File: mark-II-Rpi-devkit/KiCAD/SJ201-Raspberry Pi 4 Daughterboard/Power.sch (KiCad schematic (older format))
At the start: 36 parts, among them J1 Barrel_Jack, J5 PowerTP, Q3 AO3401A, U1 XL4501E1, U2 NCP303LSN09, U4 AMS1117-3.3, U7 MP2359

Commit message: SJ-201 v3, sent to PCB Fab. Removed USB Hub, add in I2S to Line Out
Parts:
- C1: Tempo (none) -> UCD1H221MNL1GS
- C2: Tempo (none) -> C0402C222K5RACTU
- C6: SKU 508000001 -> (none); Tempo (none) -> 25TKV330M8X10.5
- C64: Tempo (none) -> EEE-1CA471UP
- C8: SKU 508000001 -> (none)
- D14: Tempo (none) -> SS54-HF
- D15: Tempo (none) -> B5819W-TP
- FB8: Tempo (none) -> BK32164S301-T
- L1: Tempo (none) -> VCMT136E-470MN5
- L2: Tempo (none) -> BRL3225T2R2M
- PWR1: Tempo (none) -> 19-217/R6C-AL1M2VY/3T
- R27: Tempo (none) -> ERJ-2GEJ104X
- R28: Tempo (none) -> RC0402JR-07680RL
- R3: Tempo (none) -> RC0402FR-0775KL
- R4: Tempo (none) -> RC0402FR-07330KL
- R8: Tempo (none) -> RC0402FR-073K3L
- U4: value AMS1117-3.3 -> NCP565; Link (none) -> https://lcsc.com/product-detail/Dropout-Regulators-LDO_ON-S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; MPN AMS1117-3.3 -> NCP565ST12T3G; Tempo (none) -> NCP565ST12T3G
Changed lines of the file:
@@
 Sheet 2 6
 Title "Power"
-Date "2020-09-26"
-Rev "0.67b"
+Date "2020-10-02"
+Rev "0.67c"
 Comp "Mycroft"
 Comment1 "Power Converter"
@@
 F 5 "https://lcsc.com/product-detail/Power-Inductors_TDG-TMAX-1365-470-M_C429835.html" V 4275 3075 50  0001 C CNN "Link"
 F 6 "C429835" H 4275 3075 50  0001 C CNN "LCSC"
+F 7 "VCMT136E-470MN5" H 4275 3075 50  0001 C CNN "Tempo"
 	1    4275 3075
 	0    -1   -1   0
@@
 F 4 "0402WGF3301TCE" H 5475 3525 50  0001 C CNN "MPN"
 F 5 "C25890" H 5475 3525 50  0001 C CNN "LCSC"
+F 6 "RC0402FR-073K3L" H 5475 3525 50  0001 C CNN "Tempo"
 	1    5475 3525
 	-1   0    0    1
@@
 F 4 "RVT1E331M0810" H 4880 3575 20  0001 C CNN "MPN"
 F 5 "C74593-DNP" H 4850 3425 50  0001 C CNN "LCSC"
-F 6 "508000001" H 4850 3425 50  0001 C CNN "SKU"
+F 6 "25TKV330M8X10.5" H 4850 3425 50  0001 C CNN "Tempo"
 	1    4850 3425
 	1    0    0    -1
@@
 F 4 "GRM155R71A333KA01D" H 5855 3375 20  0001 C CNN "MPN"
 F 5 "C1585" H 5825 3225 50  0001 C CNN "LCSC"
-F 6 "508000001" H 5825 3225 50  0001 C CNN "SKU"
 	1    5825 3225
 	1    0    0    -1
@@
 F 5 "301010033" H 8850 1575 50  0001 C CNN "SKU"
 F 6 "C25741" H 8850 1575 50  0001 C CNN "LCSC"
+F 7 "ERJ-2GEJ104X" H 8850 1575 50  0001 C CNN "Tempo"
 	1    8850 1575
 	1    0    0    -1
@@
 P 1925 4750
 F 0 "U4" H 1925 4992 50  0000 C CNN
-F 1 "AMS1117-3.3" H 1925 4901 50  0000 C CNN
+F 1 "NCP565" H 1925 4901 50  0000 C CNN
 F 2 "Package_TO_SOT_SMD:SOT-223-3_TabPin2" H 1925 5000 50  0001 C CIN
 F 3 "" H 1925 4750 50  0001 C CNN
-F 4 "AMS1117-3.3" H 1925 4750 50  0001 C CNN "MPN"
-F 5 "C6186" H 1925 4750 50  0001 C CNN "LCSC"
+F 4 "NCP565ST12T3G" H 1925 4750 50  0001 C CNN "MPN"
+F 5 "NCP565ST12T3G" H 1925 4750 50  0001 C CNN "Tempo"
+F 6 "C6186" H 1925 4750 50  0001 C CNN "LCSC"
+F 7 "https://lcsc.com/product-detail/Dropout-Regulators-LDO_ON-Semiconductor-ON-NCP565ST12T3G_C556400.html" H 1925 4750 50  0001 C CNN "Link"
 	1    1925 4750
 	1    0    0    -1
@@
 F 6 "https://lcsc.com/product-detail/Others_TOGIALED-TJ-S1608SW6TGLC2R-A5_C192315.html" V 6650 3425 50  0001 C CNN "Link"
 F 7 "304090042" H 6650 3425 50  0001 C CNN "SKU"
+F 8 "19-217/R6C-AL1M2VY/3T" H 6650 3425 50  0001 C CNN "Tempo"
 	1    6650 3425
 	0    -1   -1   0
@@
 F 5 "Chip Resistor - Surface Mount 680Ohms ±1% 1/16W 0402 RoHS" H 6650 3175 50  0001 C CNN "Desc"
 F 6 "0402WGF6800TCE" H 6650 3175 50  0001 C CNN "MPN"
+F 7 "RC0402JR-07680RL" H 6650 3175 50  0001 C CNN "Tempo"
 	1    6650 3175
 	-1   0    0    1
@@
 F 4 "MLB3216-301P3A(f)" H 8350 1175 50  0001 C CNN "MPN"
 F 5 "C29107" H 8350 1175 50  0001 C CNN "LCSC"
+F 6 "BK32164S301-T" H 8350 1175 50  0001 C CNN "Tempo"
 	1    8350 1175
 	0    -1   1    0
@@
 F 5 "302030006" H 9280 1525 20  0001 C CNN "SKU"
 F 6 "C176671-DNP" H 9250 1375 50  0001 C CNN "LCSC"
+F 7 "EEE-1CA471UP" H 9250 1375 50  0001 C CNN "Tempo"
 	1    9250 1375
 	1    0    0    -1
@@
 F 4 "SS54F" H 3900 3250 50  0001 C CNN "MPN"
 F 5 "C22452" H 3900 3250 50  0001 C CNN "LCSC"
+F 6 "SS54-HF" H 3900 3250 50  0001 C CNN "Tempo"
 	1    3900 3250
 	0    1    1    0
@@
 F 7 "https://lcsc.com/product-detail/Aluminum-Electrolytic-Capacitors-SMD_Lelon-VZH221M1HTR-1010_C134819.html/?href=jlc-SMT" H 1600 3275 50  0001 C CNN "Link"
 F 8 "LCSC" H 1600 3275 50  0001 C CNN "Vendor"
+F 9 "UCD1H221MNL1GS" H 1600 3275 50  0001 C CNN "Tempo"
 	1    1600 3275
 	1    0    0    -1
@@
 F 4 "C25798" H 4325 6700 50  0001 C CNN "LCSC"
 F 5 "0402WGF7502TCE" H 4325 6700 50  0001 C CNN "MPN"
+F 6 "RC0402FR-0775KL" H 4325 6700 50  0001 C CNN "Tempo"
 	1    4325 6700
 	1    0    0    -1
@@
 F 4 "C86074" H 3825 6550 50  0001 C CNN "LCSC"
 F 5 "LQH32PN2R2NN0L" H 3825 6550 50  0001 C CNN "MPN"
+F 6 "BRL3225T2R2M" H 3825 6550 50  0001 C CNN "Tempo"
 	1    3825 6550
 	0    -1   -1   0
@@
 F 4 "C25778" H 4325 7050 50  0001 C CNN "LCSC"
 F 5 "0402WGF3303TCE" H 4325 7050 50  0001 C CNN "MPN"
+F 6 "RC0402FR-07330KL" H 4325 7050 50  0001 C CNN "Tempo"
 	1    4325 7050
 	-1   0    0    1
@@
 F 4 "B5819W" H 3400 6700 50  0001 C CNN "MPN"
 F 5 "C8598" H 3400 6700 50  0001 C CNN "LCSC"
+F 6 "B5819W-TP" H 3400 6700 50  0001 C CNN "Tempo"
 	1    3400 6700
 	0    1    1    0
@@
 F 6 "https://lcsc.com/product-detail/Multilayer-Ceramic-Capacitors-MLCC-SMD-SMT_2-2nF-222-10-50V_C1531.html/?href=jlc-SMT" H 3350 5200 50  0001 C CNN "Link"
 F 7 "LCSC" H 3350 5200 50  0001 C CNN "Vendor"
+F 8 "C0402C222K5RACTU" H 3350 5200 50  0001 C CNN "Tempo"
 	1    3350 5200
 	-1   0    0    -1

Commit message: Rev4 Update - Add in Coral TPU, TAS5806, remove I2S * MAX9744. Change Attiny to Attin1614
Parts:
- removed C2: 2.2NF, Capacitor_SMD:C_0402_1005Metric, symbol Device:C_Small
- removed C9: 1NF, Capacitor_SMD:C_0402_1005Metric, symbol Device:C_Small
- removed R2: 10k, Resistor_SMD:R_0402_1005Metric, symbol Device:R_Small
- removed TP25: TestPoint, TestPoint:TestPoint_Pad_D2.0mm, symbol Connector:TestPoint
- removed U2: NCP303LSN09, Package_TO_SOT_SMD:SOT-23-5, symbol user:NCP303LSN30
- added C66: 1uF, Capacitor_Tantalum_SMD:CP_EIA-3216-10_Kemet-I, symbol Device:CP1_Small
- added C67: 470uF, Capacitor_Tantalum_SMD:CP_EIA-7343-15_Kemet-W, symbol Device:CP
- added R51: 3.3K, Resistor_SMD:R_0402_1005Metric, symbol Device:R_Small
- added TP12v1: TestPoint, TestPoint:TestPoint_Pad_D2.0mm, symbol Connector:TestPoint
- added U12: TPS75933KTT, Package_TO_SOT_SMD:TO-263-5_TabPin3, symbol user:TPS759xxx
- J5: footprint Connector_PinHeader_2.54mm:PinHeader_2x04_P2.54mm_Vertical -> Connector_PinHeader_1.27mm:PinHeader_1x06_P1.27mm_Vertical_SMD_Pin1Left; symbol Connector_Generic:Conn_02x04_Odd_Even -> Connector_Generic:Conn_02x03_Odd_Even
- U4: value NCP565 -> AMS1117-3.3; MPN NCP565ST12T3G -> (none); Tempo NCP565ST12T3G -> (none)
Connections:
- net labels added: Enable1V
- net labels removed: 1v0Enable, PGND, PVDD
- wire segments 82 -> 88
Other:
- note added: "3.3v LDO High Power for Coral TPU"
- note removed: "Power on Delay 1v0 Buck"

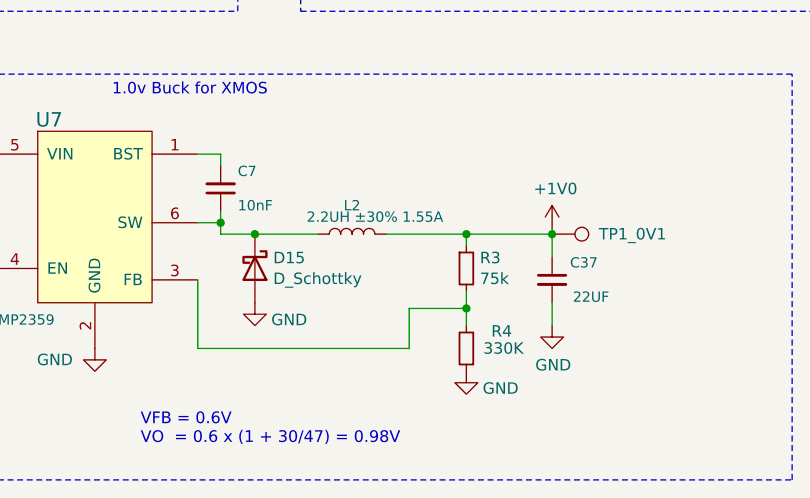
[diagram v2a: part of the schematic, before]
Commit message: Rev4 Update - fix some wiring, export for printing Rev 4
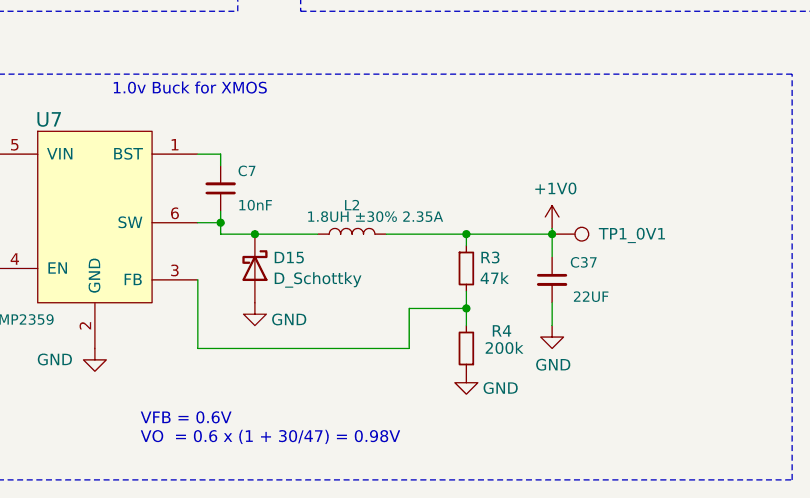
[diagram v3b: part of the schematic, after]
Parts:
- C1: LCSC C134819-DNP -> C249500
- C6: LCSC C74593-DNP -> C286135
- C64: LCSC C176671-DNP -> C176671
- J1: footprint user:BarrelJack_Vertical -> Connector_BarrelJack:BarrelJack_Horizontal
- L2: value 2.2UH ±30% 1.55A -> 1.8UH ±30% 2.35A; footprint Inductor_SMD:L_1210_3225Metric -> Inductor_SMD:L_Bourns-SRN4018; LCSC C86074 -> (none); MPN LQH32PN2R2NN0L -> SRR4018-1R8Y; Tempo BRL3225T2R2M -> (none)
- R3: value 75k -> 47k; LCSC C25798 -> C25792; MPN 0402WGF7502TCE -> (none); Tempo RC0402FR-0775KL -> (none)
- R4: value 330K -> 200k; LCSC C25778 -> C25764; MPN 0402WGF3303TCE -> (none); Tempo RC0402FR-07330KL -> (none)
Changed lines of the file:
@@
 Sheet 2 7
 Title "Power"
-Date "2020-11-18"
-Rev "rev4 - 0.01"
+Date "2020-11-22"
+Rev "Rev4 - 0.03"
 Comp "Mycroft"
-Comment1 "SJ201 r4.01"
+Comment1 "SJ-201-R4"
 Comment2 ""
 Comment3 ""
@@
 F 3 "https://file.elecfans.com/web1/M00/A2/5C/pIYBAF1Kg6yAV45LAAQT68kiml8120.pdf?filename=RVT_Heyue.pdf" H 4850 3425 50  0001 C CNN
 F 4 "RVT1E331M0810" H 4880 3575 20  0001 C CNN "MPN"
-F 5 "C74593-DNP" H 4850 3425 50  0001 C CNN "LCSC"
+F 5 "C286135" H 4850 3425 50  0001 C CNN "LCSC"
 F 6 "25TKV330M8X10.5" H 4850 3425 50  0001 C CNN "Tempo"
 	1    4850 3425
@@
 F 0 "J1" H 5707 1700 50  0000 C CNN
 F 1 "Barrel_Jack" H 5707 1609 50  0000 C CNN
-F 2 "user:BarrelJack_Vertical" H 5700 1335 50  0001 C CNN
+F 2 "Connector_BarrelJack:BarrelJack_Horizontal" H 5700 1335 50  0001 C CNN
 F 3 "https://datasheet.lcsc.com/szlcsc/2002271745_XKB-Connectivity-DC-012-5A-2-0_C381117.pdf" H 5700 1335 50  0001 C CNN
 F 4 "DC-012-5A-2.0" H 5650 1375 50  0001 C CNN "MPN"
@@
 F 4 "SMD CAP Aluminum 470uF-16V;D8.0*H10.2mm" H 9280 1525 20  0001 C CNN "MPN"
 F 5 "302030006" H 9280 1525 20  0001 C CNN "SKU"
-F 6 "C176671-DNP" H 9250 1375 50  0001 C CNN "LCSC"
+F 6 "C176671" H 9250 1375 50  0001 C CNN "LCSC"
 F 7 "EEE-1CA471UP" H 9250 1375 50  0001 C CNN "Tempo"
 	1    9250 1375
@@
 F 3 "" H 1600 3275 50  0001 C CNN
 F 4 "VZH221M1HTR-1010" H 1630 3425 20  0001 C CNN "MPN"
-F 5 "C134819-DNP" H 1600 3275 50  0001 C CNN "LCSC"
+F 5 "C249500" H 1600 3275 50  0001 C CNN "LCSC"
 F 6 " " H 1600 3275 50  0001 C CNN "SKU"
 F 7 "https://lcsc.com/product-detail/Aluminum-Electrolytic-Capacitors-SMD_Lelon-VZH221M1HTR-1010_C134819.html/?href=jlc-SMT" H 1600 3275 50  0001 C CNN "Link"
@@
 AR Path="/5EAAC9A5/5F44B374" Ref="R3"  Part="1"
 F 0 "R3" H 4384 6746 50  0000 L CNN
-F 1 "75k" H 4384 6655 50  0000 L CNN
+F 1 "47k" H 4384 6655 50  0000 L CNN
 F 2 "Resistor_SMD:R_0402_1005Metric" H 4325 6700 50  0001 C CNN
 F 3 "~" H 4325 6700 50  0001 C CNN
-F 4 "C25798" H 4325 6700 50  0001 C CNN "LCSC"
-F 5 "0402WGF7502TCE" H 4325 6700 50  0001 C CNN "MPN"
-F 6 "RC0402FR-0775KL" H 4325 6700 50  0001 C CNN "Tempo"
+F 4 "C25792" H 4325 6700 50  0001 C CNN "LCSC"
 	1    4325 6700
 	1    0    0    -1
@@
 AR Path="/5EAAC9A5/5F44B395" Ref="L2"  Part="1"
 F 0 "L2" V 3950 6550 45  0000 C CNN
-F 1 "2.2UH ±30% 1.55A" V 3900 6450 45  0000 C CNN
-F 2 "Inductor_SMD:L_1210_3225Metric" H 3825 6550 60  0001 C CNN
-F 3 "https://datasheet.lcsc.com/szlcsc/Murata-Electronics-LQH32PN2R2NN0L_C86074.pdf" H 3825 6550 60  0001 C CNN
-F 4 "C86074" H 3825 6550 50  0001 C CNN "LCSC"
-F 5 "LQH32PN2R2NN0L" H 3825 6550 50  0001 C CNN "MPN"
-F 6 "BRL3225T2R2M" H 3825 6550 50  0001 C CNN "Tempo"
+F 1 "1.8UH ±30% 2.35A" V 3900 6450 45  0000 C CNN
+F 2 "Inductor_SMD:L_Bourns-SRN4018" H 3825 6550 60  0001 C CNN
+F 3 "" H 3825 6550 60  0001 C CNN
+F 4 "SRR4018-1R8Y" H 3825 6550 50  0001 C CNN "MPN"
 	1    3825 6550
 	0    -1   -1   0
@@
 AR Path="/5EAAC9A5/5F44B3B5" Ref="R4"  Part="1"
 F 0 "R4" H 4125 6975 50  0000 L CNN
-F 1 "330K" H 4075 7050 50  0000 L CNN
+F 1 "200k" H 4075 7050 50  0000 L CNN
 F 2 "Resistor_SMD:R_0402_1005Metric" H 4325 7050 50  0001 C CNN
 F 3 "~" H 4325 7050 50  0001 C CNN
-F 4 "C25778" H 4325 7050 50  0001 C CNN "LCSC"
-F 5 "0402WGF3303TCE" H 4325 7050 50  0001 C CNN "MPN"
-F 6 "RC0402FR-07330KL" H 4325 7050 50  0001 C CNN "Tempo"
+F 4 "C25764" H 4325 7050 50  0001 C CNN "LCSC"
 	1    4325 7050
 	-1   0    0    1

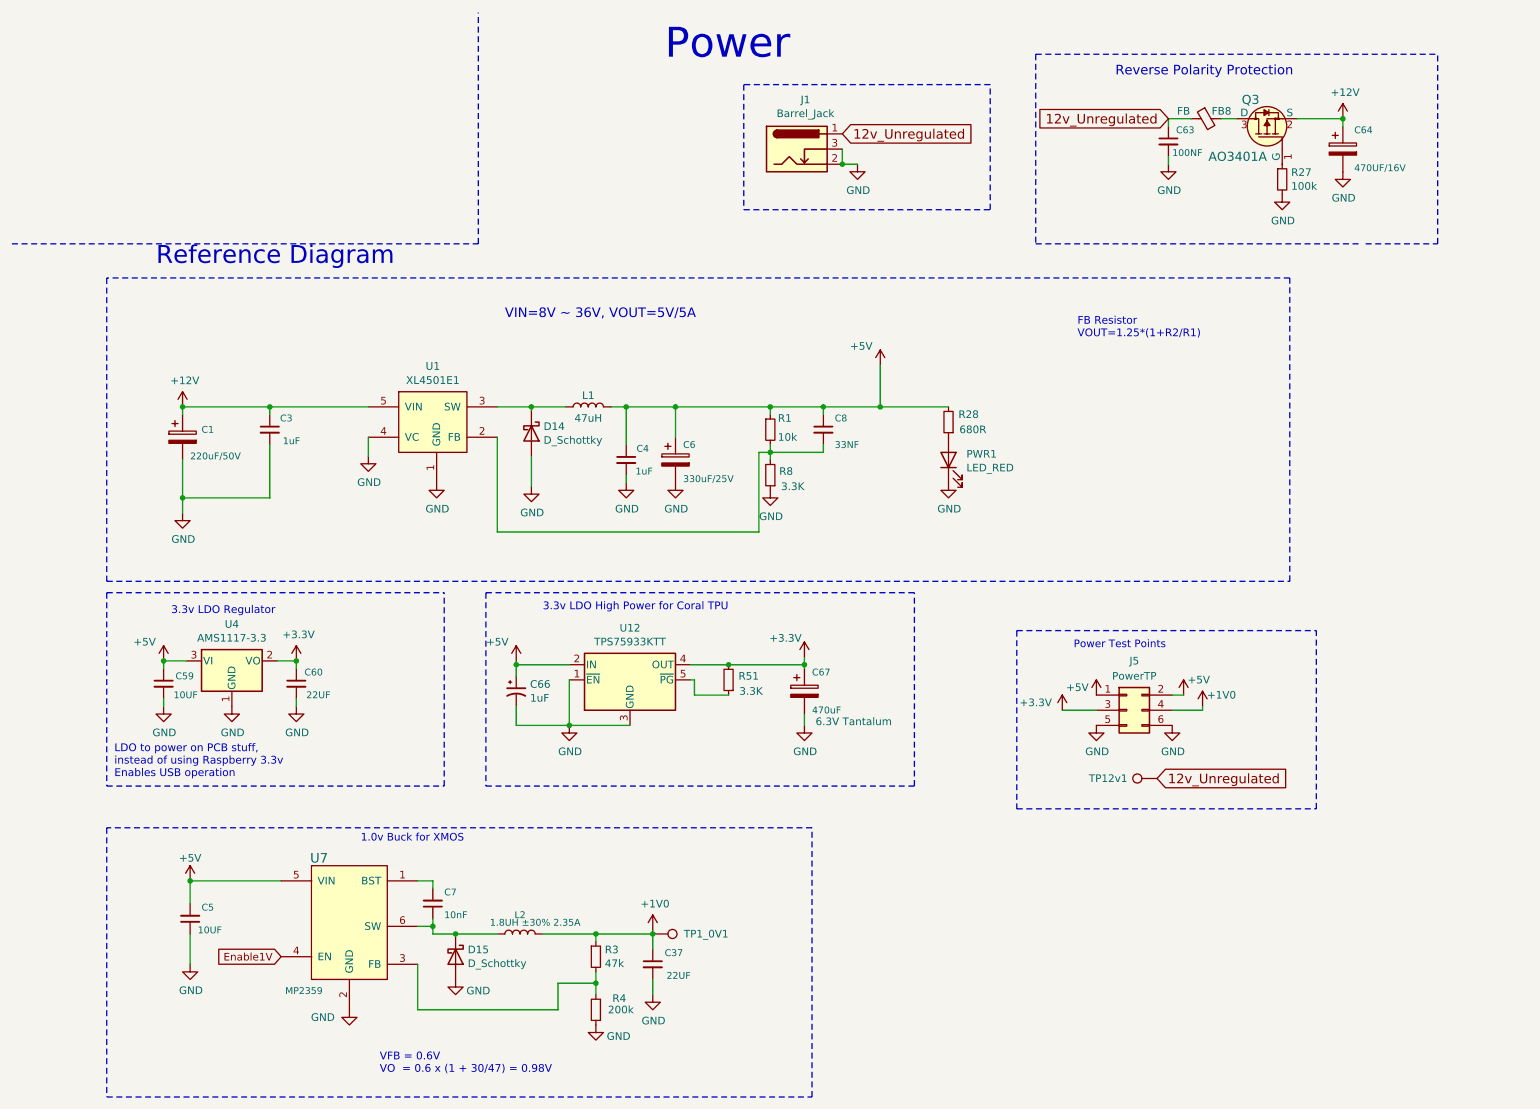
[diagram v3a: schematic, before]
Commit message: SJ-201-R6 for FAB - removed buffer IC
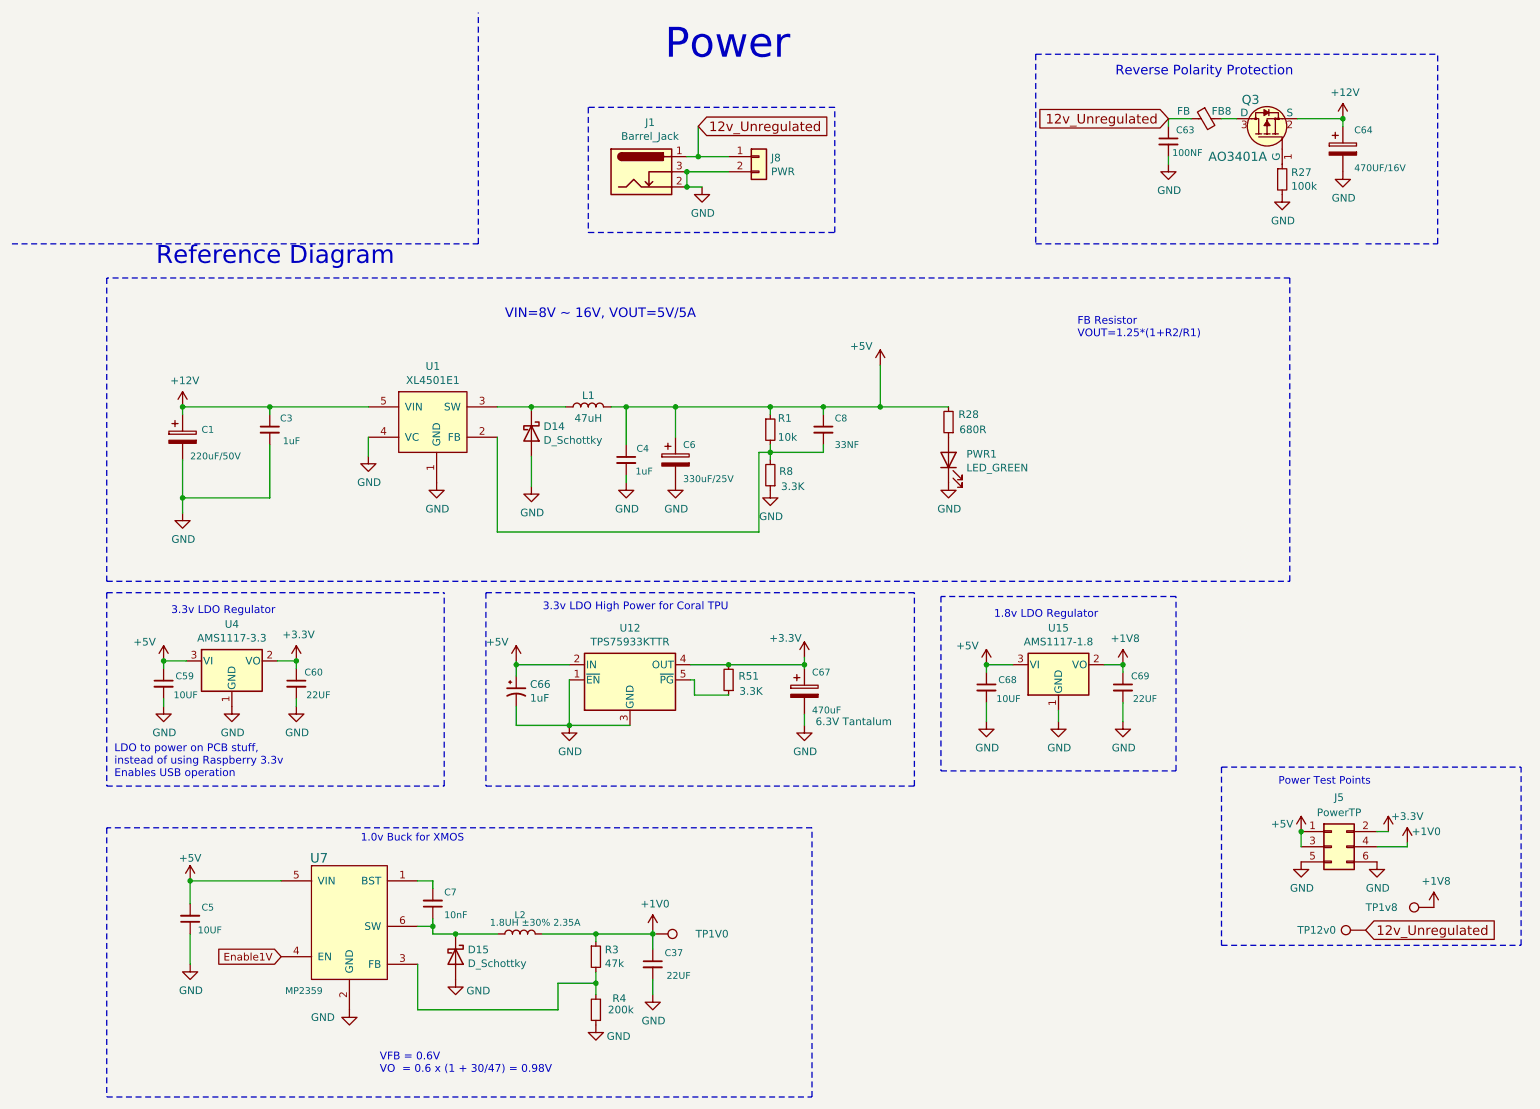
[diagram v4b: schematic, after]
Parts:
- added C68: 10UF, Capacitor_SMD:C_0402_1005Metric, symbol Device:C_Small
- added C69: 22UF, Capacitor_SMD:C_0603_1608Metric, symbol Device:C_Small
- added J8: PWR, Connector_PinHeader_2.54mm:PinHeader_1x02_P2.54mm_Vertical, symbol Connector_Generic:Conn_01x02
- added TP1v8: TestPoint, TestPoint:TestPoint_Pad_D2.0mm, symbol Connector:TestPoint
- added U15: AMS1117-1.8, Package_TO_SOT_SMD:SOT-223-3_TabPin2, symbol Regulator_Linear:AMS1117-1.8
- C1: LCSC C249500 -> C134732; Link https://lcsc.com/product-detail/Aluminum-Electrolytic-Capac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 -> https://datasheet.lcsc.com/szlcsc/Lelon-VE-221M1HTR-1010_C1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; MPN VZH221M1HTR-1010 -> VE-221M1HTR-1010; Tempo UCD1H221MNL1GS -> (none)
- C66: LCSC C140386 -> C7174; Link (none) -> https://lcsc.com/product-detail/Tantalum-Capacitors_AVX-TAJ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; MPN CA45-A-16V-1uF-K -> TAJA105K016RNJ
- C67: LCSC C156460 -> C79114; MPN T520D477M006ATE025 -> 6TPE470MAZU
- J1: LCSC C381117 -> C381116; MPN DC-012-5A-2.0 -> DC-005-5A-2.0
- J5: LCSC (none) -> DNP
- L1: LCSC C429835 -> C497913; Link https://lcsc.com/product-detail/Power-Inductors_TDG-TMAX-13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 -> https://lcsc.com/product-detail/Power-Inductors_YJYCOIN-YSP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; MPN TMAX-1365-470-M -> YSPI1365-470M; Tempo VCMT136E-470MN5 -> (none)
- L2: Link (none) -> https://www.digikey.com/en/products/detail/bourns-inc/SRR40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
- PWR1: value LED_RED -> LED_GREEN; LCSC C2286 -> C72043; Link https://lcsc.com/product-detail/Others_TOGIALED-TJ-S1608SW6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 -> https://lcsc.com/product-detail/Light-Emitting-Diodes-LED_0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; MPN 19-217-R6C-AL1M2VY-3T -> 19-217/GHC-YR1S2/3T; SKU 304090042 -> (none); Tempo 19-217/R6C-AL1M2VY/3T -> (none)
- Q3: LCSC C15127 -> C306862
- R3: MPN (none) -> 0402WGF4702TCE
- R4: MPN (none) -> 0402WGF2003TCE
- U1: Link (none) -> https://lcsc.com/product-detail/DC-DC-Converters_XLSEMI-XL4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
- U12: value TPS75933KTT -> TPS75933KTTR; Link (none) -> https://www.digikey.com/en/products/detail/texas-instrument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; MPN (none) -> TPS75933KTTR
- U4: MPN (none) -> AMS1117-3.3-DNP
- U7: Link (none) -> https://www.mouser.com/ProductDetail/Monolithic-Power-Syste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
- renumbered TP12v1 to TP12v0, TP1_0V1 to TP1V0
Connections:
- net +3V3: now also J5.2 (Pin_2); no longer J5.3 (Pin_3)
- net +5V: now also J5.3 (Pin_3), C68.1, U15.3 (VI); no longer J5.2 (Pin_2)
- net 12v_Unregulated: now also J8.1 (Pin_1)
- net GND: now also C68.2, C69.2, J8.2 (Pin_2), U15.1 (GND)
- new net +1V8: C69.1, TP1v8.1, U15.2 (VO)
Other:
- note added: "1.8v LDO Regulator"
- note added: "VIN=8V ~~ 16V, VOUT=5V/5A"
- note removed: "VIN=8V ~~ 36V, VOUT=5V/5A"
- moved on the sheet: J1, J5, TP12v0
